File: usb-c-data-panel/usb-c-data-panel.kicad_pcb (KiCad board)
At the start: 2 copper layers, 25 x 14.1 mm, 24 parts

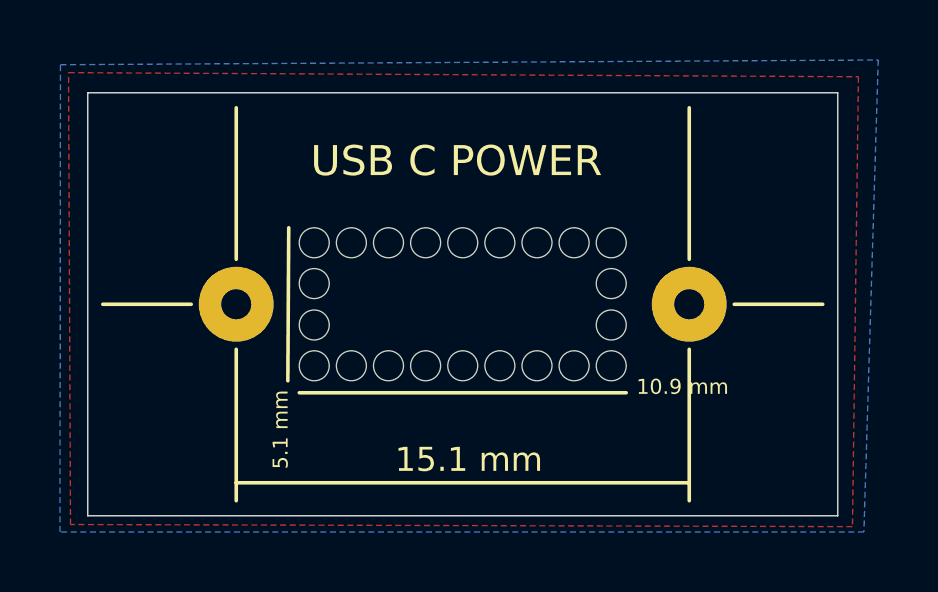
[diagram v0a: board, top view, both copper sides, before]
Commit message: usb c data panel pcb
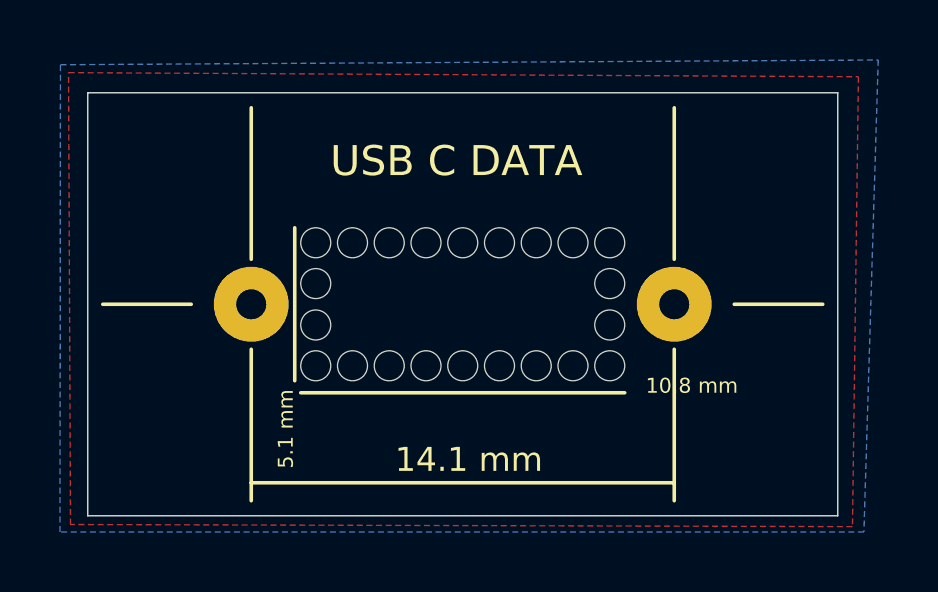
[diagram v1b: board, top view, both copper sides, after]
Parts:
- moved REF** 0.50 mm to (119.5, 107.0)
- moved REF** 0.50 mm to (105.5, 107.0)
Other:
- board text added: "10.8 mm"
- board text added: "14.1 mm"
- board text added: "USB C DATA"
- board text removed: "10.9 mm"
- board text removed: "15.1 mm"
- board text removed: "USB C POWER"
